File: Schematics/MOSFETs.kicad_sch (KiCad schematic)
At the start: 54 parts, among them Q3 ISC030N10NM6, Q4 ISC030N10NM6, Q5 ISC030N10NM6, Q6 ISC030N10NM6, Q7 ISC030N10NM6, Q8 ISC030N10NM6

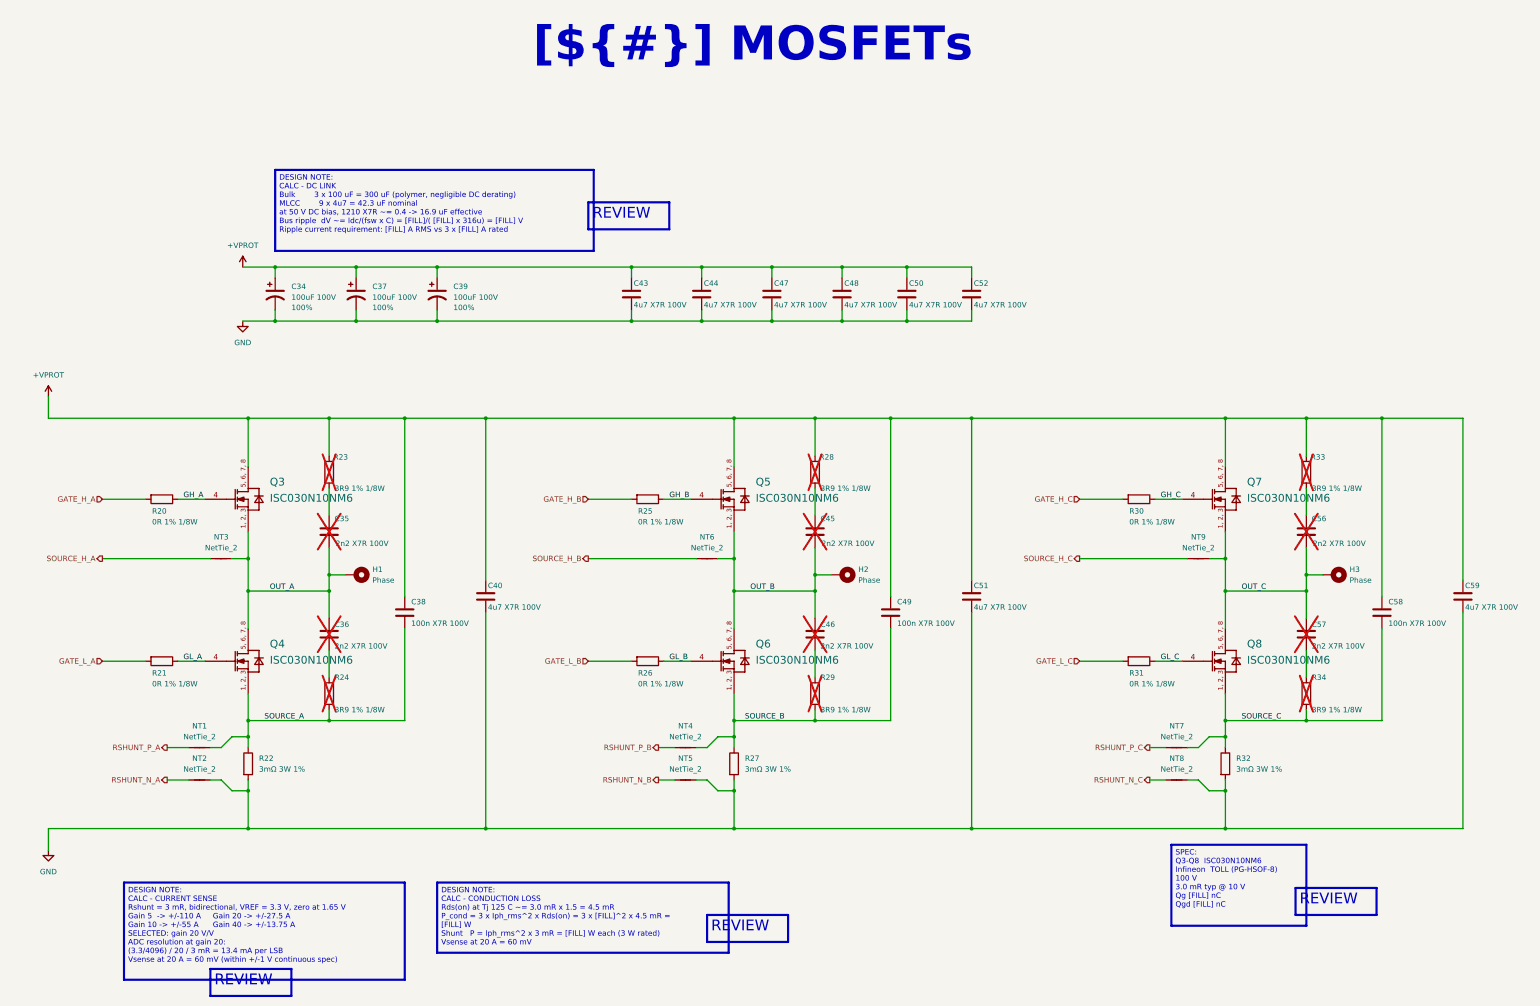
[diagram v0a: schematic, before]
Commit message: Clean up schematic design notes; export schematic and PCB artwork PDFs
- Remove firmware-only notes (boot sequence, calibration procedure,
  firmware SPI/PWM settings) and template/empty text; keep hardware facts
- Tighten wording of all DESIGN/SPEC/ASSEMBLY/REV 1 notes and resize
  boxes so no note text wraps or overflows
- Re-export schematic PDF
- Add PCB artwork PDFs (combined and one per layer: silk, paste, mask,
  L1-L6 copper), board outline on every page

Co-Authored-By: Claude Opus 5.5 <noreply@anthropic.com>
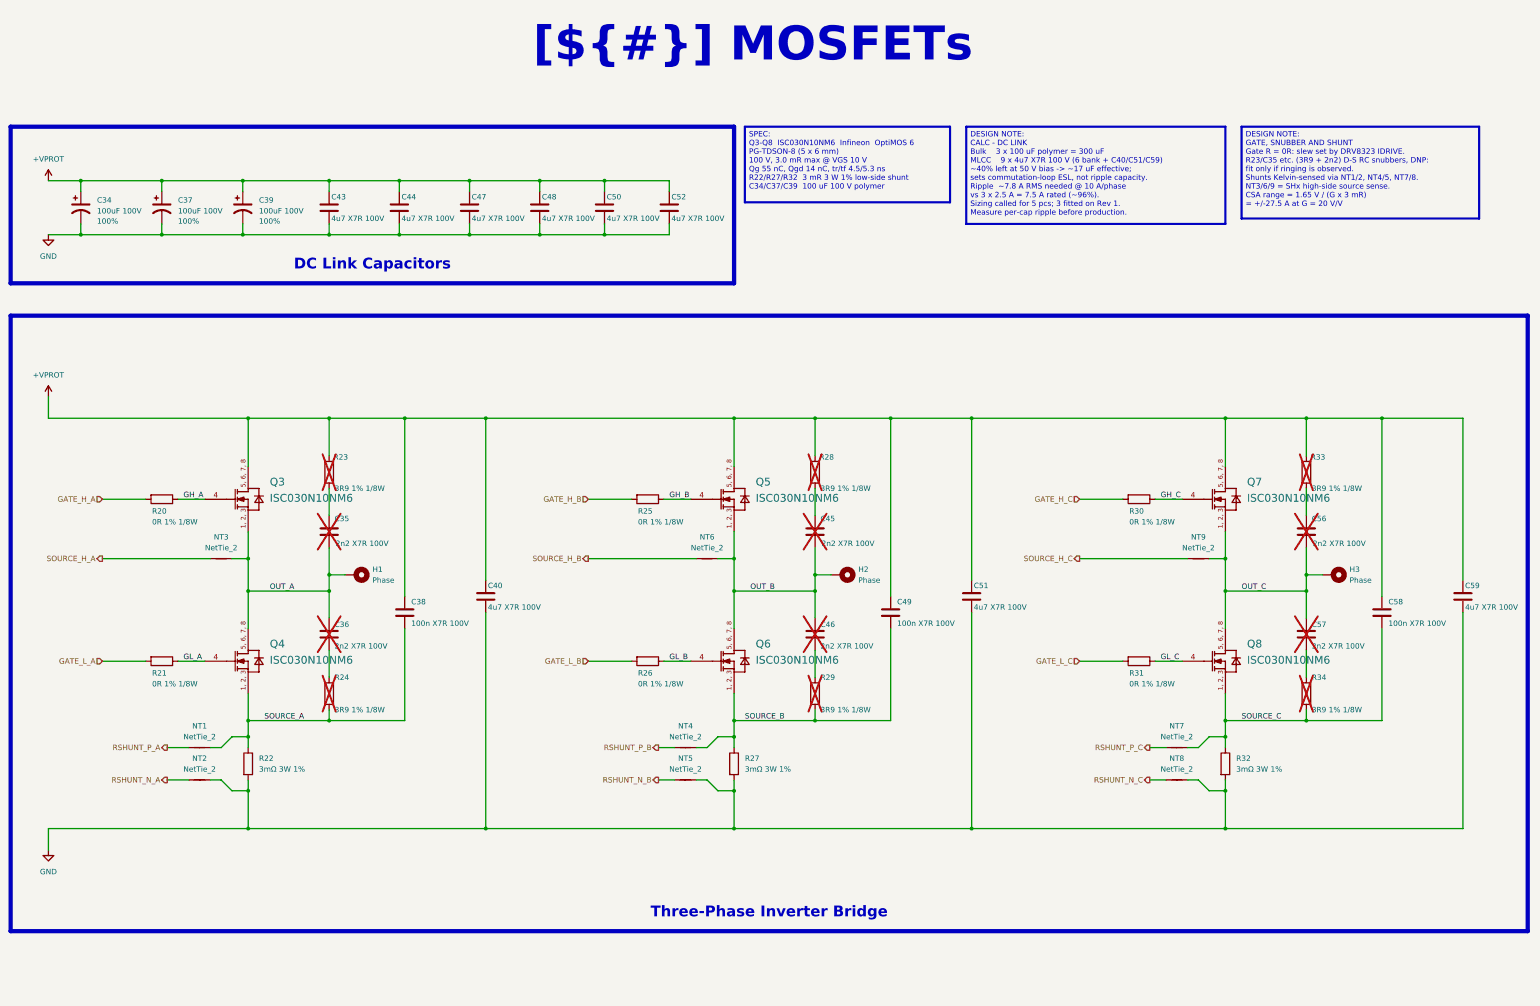
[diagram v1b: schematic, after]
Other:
- company: (none) -> ${COMPANY}
- title: (none) -> MOSFETs
- moved on the sheet: C34, C37, C39, C43, C44, C47, C48, C50, C52
